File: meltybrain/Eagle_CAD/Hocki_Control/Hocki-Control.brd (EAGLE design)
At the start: 90 x 46 mm, 128 parts, among them J1 SM03B-SRSS-TB(LF)(SN), J2 SM03B-SRSS-TB(LF)(SN), J3 SM03B-SRSS-TB(LF)(SN), J4 SM04B-SRSS-TB(LF)(SN), J5 SM04B-SRSS-TB(LF)(SN), U1 TEENSY_4.1, U10 TLV3502AIDCNR, U11 NL27WZ32USG, U12 NL27WZ32USG, U13 HMC1052L-TR, U14 LMV358, U15 IRF7509, U16 TMUX1219DCKR, U17 LMV358, U18 LMV358, U19 AP2210K-3.3TRG1, U2 ADXL375, U20 AP2210K-5.0TRG1, U21 AP63200, U22 74AHC1G04GW,125, U23 LDL212PU50R, U3 ADXL375, U4 ADXL375, U5 ADXL375, U6 LMH6612MAX/NOPB, U7 LMH6612MAX/NOPB, U8 LMH6612MAX/NOPB, U9 LMH6612MAX/NOPB

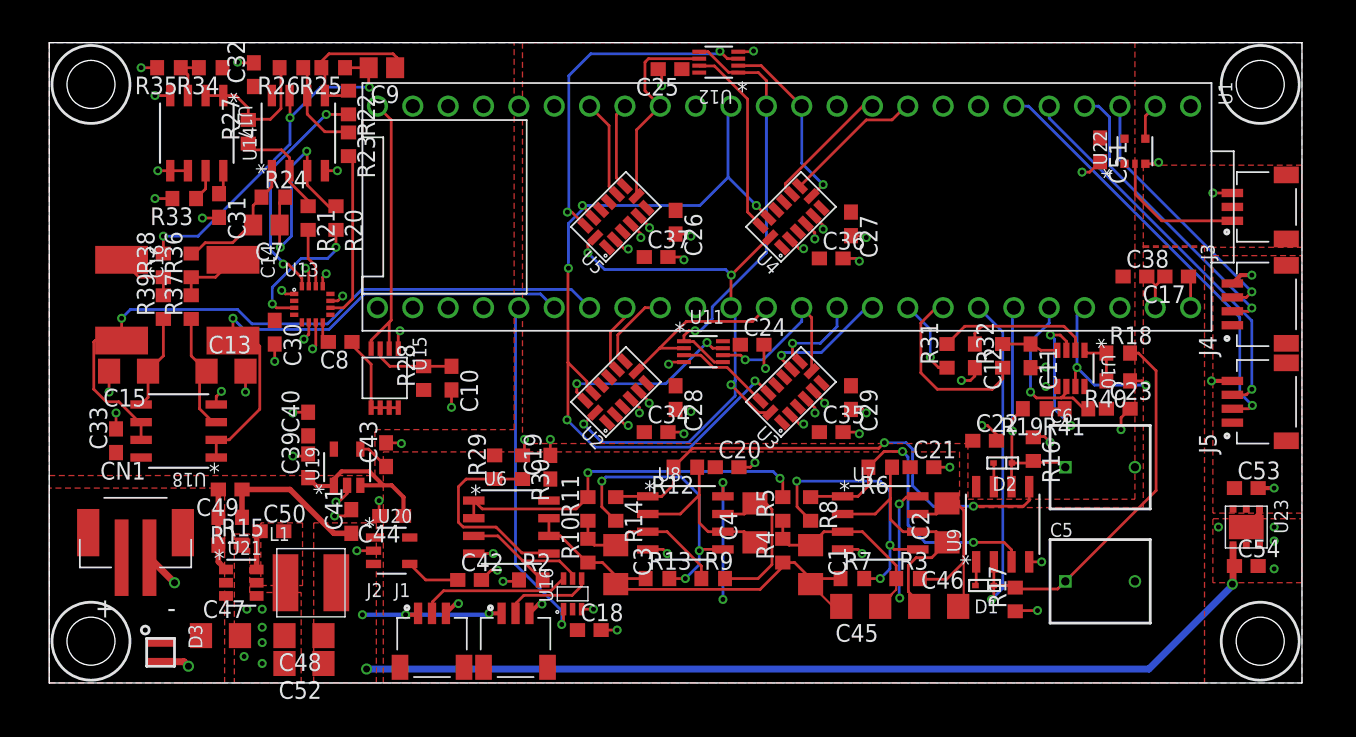
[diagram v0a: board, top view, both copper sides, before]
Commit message: control schematic done
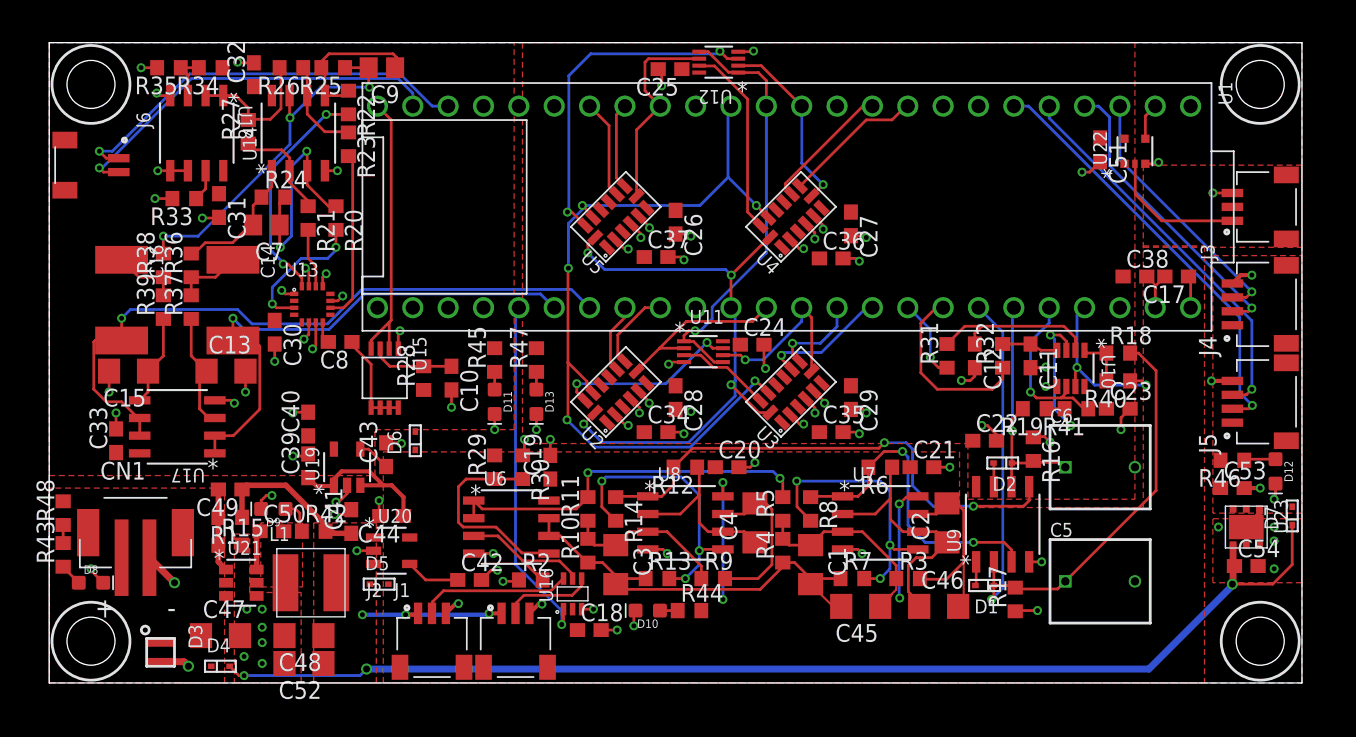
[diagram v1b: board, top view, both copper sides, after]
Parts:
- added D10, D11, D12, D13, D8, D9: GREEN, SparkFun-LED:LED-0603
- added D4, D5, D6, D7: BAS581-02V-V-G-08, Hocki_Library:SOD-523
- added J6: SM02B-SRSS-TB(LF)(SN), Hocki_Library:SM02B-SRSS-TB(LF)(SN)
- added R42: 499, rcl:R0603
- added R43, R48: 665, rcl:R0603
- added R44, R46: 330, rcl:R0603
- added R45, R47: 169, rcl:R0603
- C1, C13, C15, C2, C3, C4, C45, C46: value 47n -> 47nF
- C11, C12, C39, C41, C54: value 1u -> 1uF
- C14, C16: value 0.18u -> 0.18uF
- C17, C18, C19, C20, C21, C22, C23, C24, C25, C26, C27, C28, C29, C30, C31, C32, C33, C34, C35, C36, C37, C38, C50: value 0.1u -> 0.1uF
- C40, C44: value 2.2u -> 2.2uF
- C42, C43, C49: value 100p -> 100pF
- C47: value 10u -> 10uF
- C48, C52: value 22u -> 22uF
- C5, C6: value 62n -> 62nF
- C53: value 4.7u -> 4.7uF
- C7, C9: value 1000p -> 1000pF
- C8: value .1u -> .1uF
- moved U18 21.4 mm to (-41.4, 12.3), turned to 270 degrees
- moved U17 21.1 mm to (-42.8, -8.80), turned to 180 degrees
- moved C53 1.00 mm to (33.0, -13.2)
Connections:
- net N$17 renamed RC_SIGNAL
- new net ESC_L: J6.1, U1.30
- new net ESC_R: J6.2, U1.31
- new net N$14: D12.A, R46.1
- new net N$15: D10.A, R44.1
- new net N$17: D11.A, R45.1
- new net N$18: D9.A, R42.1
- new net N$19: D8.A, R43.1
- new net N$20: R43.2, R48.1
- new net N$27: D13.A, R47.1
- net +24V: now also D4.1, R48.2
- net +3V3: now also D6.2, J6.S1, J6.S2, R45.2
- net +5V: now also D7.2, R46.2
- net 3.3V: now also R47.2
- net 5V: now also D5.2, D6.1, R44.2
- net 9V: now also D4.2, D5.1, D7.1, R42.2
- net GND: now also D10.C, D11.C, D12.C, D13.C, D8.C, D9.C, U18.5, U18.6; no longer U17.5, U17.6
- net MAG_FILT_A: now also U17.1, U17.2; no longer U18.1, U18.2
- net MAG_FILT_B: now also U17.6, U17.7; no longer U18.6, U18.7
- net N$23: now also U18.3; no longer U17.3
- net N$24: now also U18.7; no longer U17.7
- net N$26: now also U17.3; no longer U18.3
- net N$30: now also U17.5; no longer U18.5
- net VREF/2: now also U18.1, U18.2; no longer U17.1, U17.2
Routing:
- net ESC_L: track 0.00 -> 29.9 mm, vias 0 -> 1
- net ESC_R: track 0.00 -> 28.1 mm, vias 0 -> 1
- net 9V: track 89.8 -> 108.1 mm, vias 5 -> 6
- net GND: track 111.7 -> 119.5 mm, vias 90 -> 96
- net N$18: track 0.00 -> 2.51 mm
- net N$14: track 0.00 -> 2.28 mm
- net +3V3: track 1.78 -> 0.00 mm
- net N$19: track 0.00 -> 1.62 mm
- net N$20: track 0.00 -> 1.30 mm
- net N$27: track 0.00 -> 1.27 mm
- net N$17: track 0.00 -> 1.27 mm
- net N$15: track 0.00 -> 1.27 mm

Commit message: Edited silkscreen and made minor changes to IR Receiver silkscreen and schematic
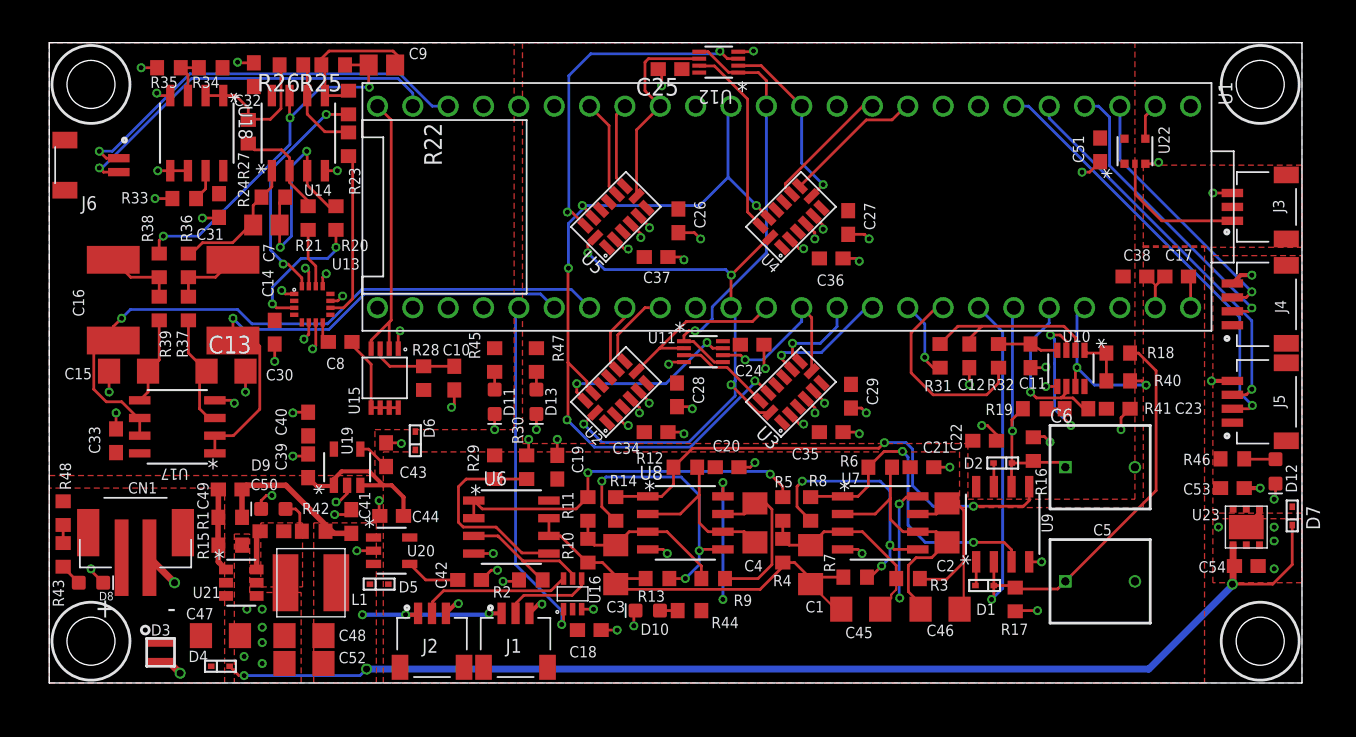
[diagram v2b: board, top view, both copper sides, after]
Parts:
- moved C16 0.60 mm to (-47.4, 0.30)
- moved C19 0.50 mm to (-15.5, -11.7)
- moved R31 0.50 mm to (12.0, -3.70)
- moved C12 0.40 mm to (14.1, -3.70)
- moved R39 0.32 mm to (-44.1, -0.30)
- moved R38 0.30 mm to (-44.1, 2.80)
- moved R30 0.30 mm to (-17.7, -11.7)
- moved R32 0.30 mm to (16.2, -3.70)
- moved R37 0.22 mm to (-42.0, -0.30)
- moved C26 0.22 mm to (-6.80, 6.00)
- moved C28 0.22 mm to (-6.90, -6.50)
- moved C27 0.22 mm to (5.40, 5.88)
- moved C46 0.22 mm to (12.0, -21.9)
- moved R7 0.22 mm to (5.90, -19.6)
- moved C10 0.20 mm to (-22.9, -5.30)
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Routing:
- net N$22: track 13.1 -> 14.3 mm
- net N$7: track 20.1 -> 19.2 mm
- net 10K_REF: track 12.5 -> 13.1 mm

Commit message: Edited LED board to add 3d packages.  Made cosmetic changes to Control in preparation for design review
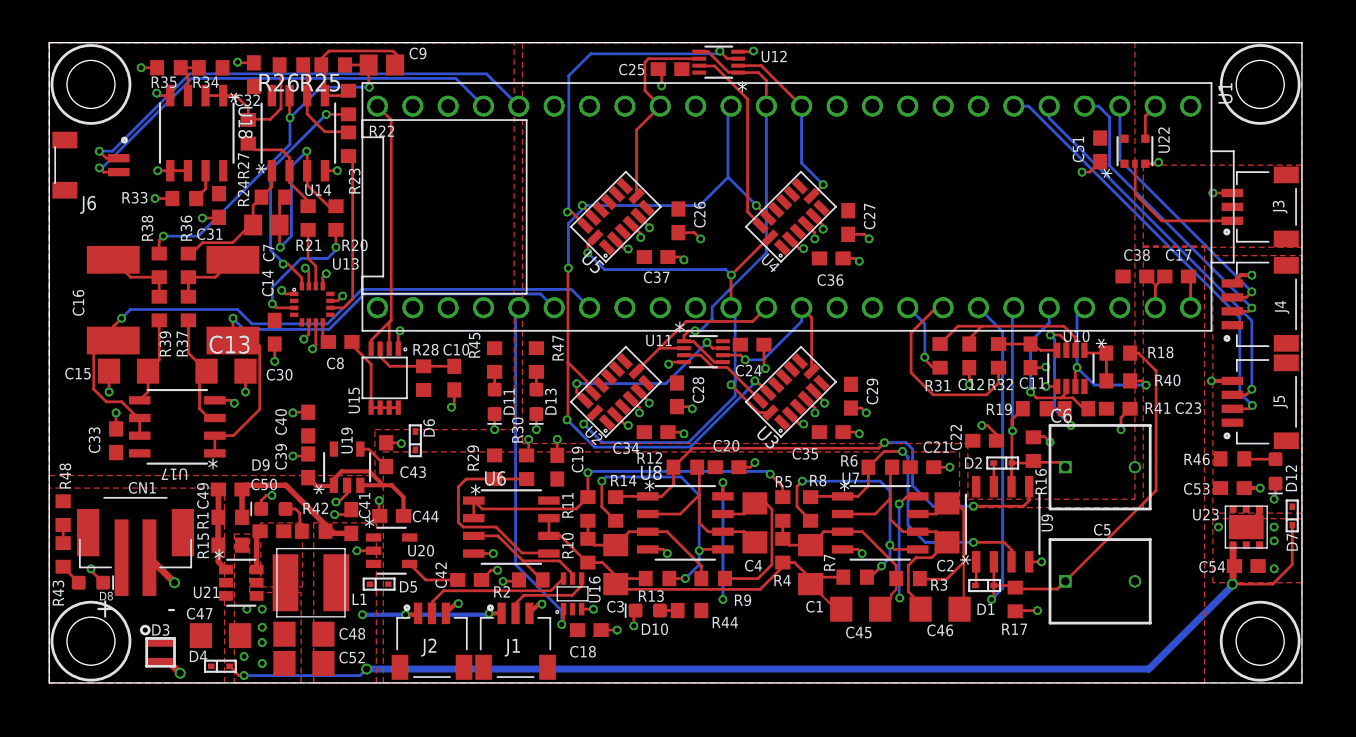
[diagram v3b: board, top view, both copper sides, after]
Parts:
- moved C48 0.10 mm to (-33.7, -23.7)
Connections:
- removed net INT1A: U1.41, U2.8
- removed net INT1B: U1.40, U2.9
- removed net INT2A: U1.16, U3.8
- removed net INT2B: U1.17, U3.9
- removed net INT3A: U1.7, U4.8
- removed net INT3B: U1.8, U4.9
- removed net INT4A: U1.25, U5.8
- removed net INT4B: U1.26, U5.9
- net 9V: now also U23.6
- net ESC_L: now also U1.28; no longer U1.30
- net ESC_R: now also U1.29; no longer U1.31
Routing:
- net INT3A: track 10.1 -> 0.00 mm
- net INT3B: track 9.50 -> 0.00 mm
- net INT2B: track 9.27 -> 0.00 mm, vias 1 -> 0
- net INT4B: track 7.14 -> 0.00 mm
- net INT2A: track 6.57 -> 0.00 mm, vias 1 -> 0
- net INT4A: track 6.26 -> 0.00 mm
- net INT1A: track 5.97 -> 0.00 mm
- net ESC_L: track 29.9 -> 35.0 mm
- net INT1B: track 5.05 -> 0.00 mm
- net ESC_R: track 28.1 -> 32.6 mm

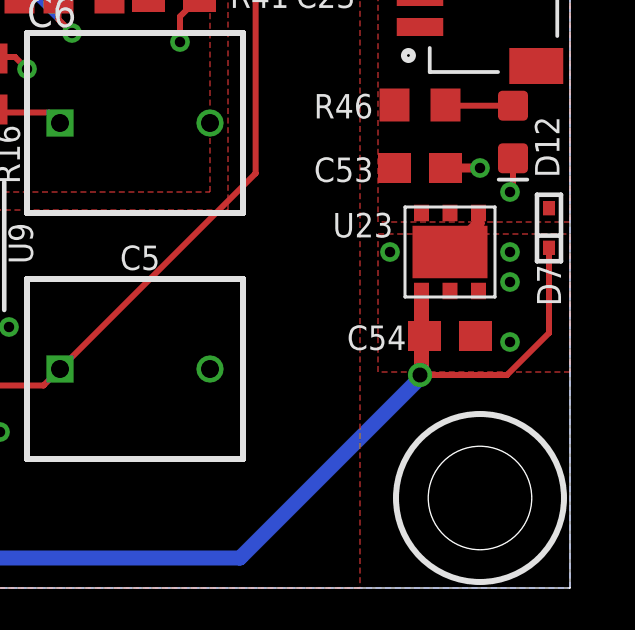
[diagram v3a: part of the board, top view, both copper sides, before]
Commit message: enable of ldo routed
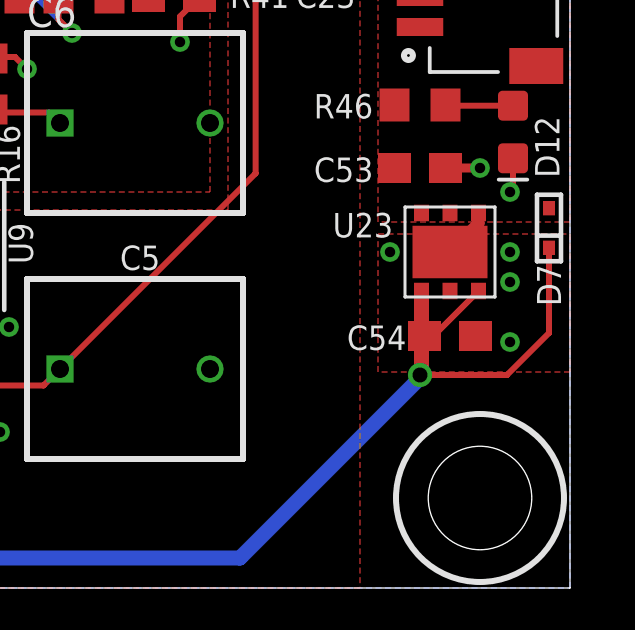
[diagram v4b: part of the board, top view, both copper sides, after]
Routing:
- net 9V: track 108.1 -> 110.7 mm
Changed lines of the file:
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@@
 <contactref element="R42" pad="2"/>
 <contactref element="U23" pad="6"/>
-<wire x1="33.05" y1="-17.3" x2="34.95" y2="-17.3" width="0" layer="19" extent="1-1"/>
+<wire x1="34.95" y1="-17.3" x2="33.35" y2="-18.9" width="0.2" layer="1"/>
+<wire x1="33.35" y1="-18.9" x2="33.05" y2="-18.9" width="0.2" layer="1"/>
 </signal>
 <signal name="N$8">

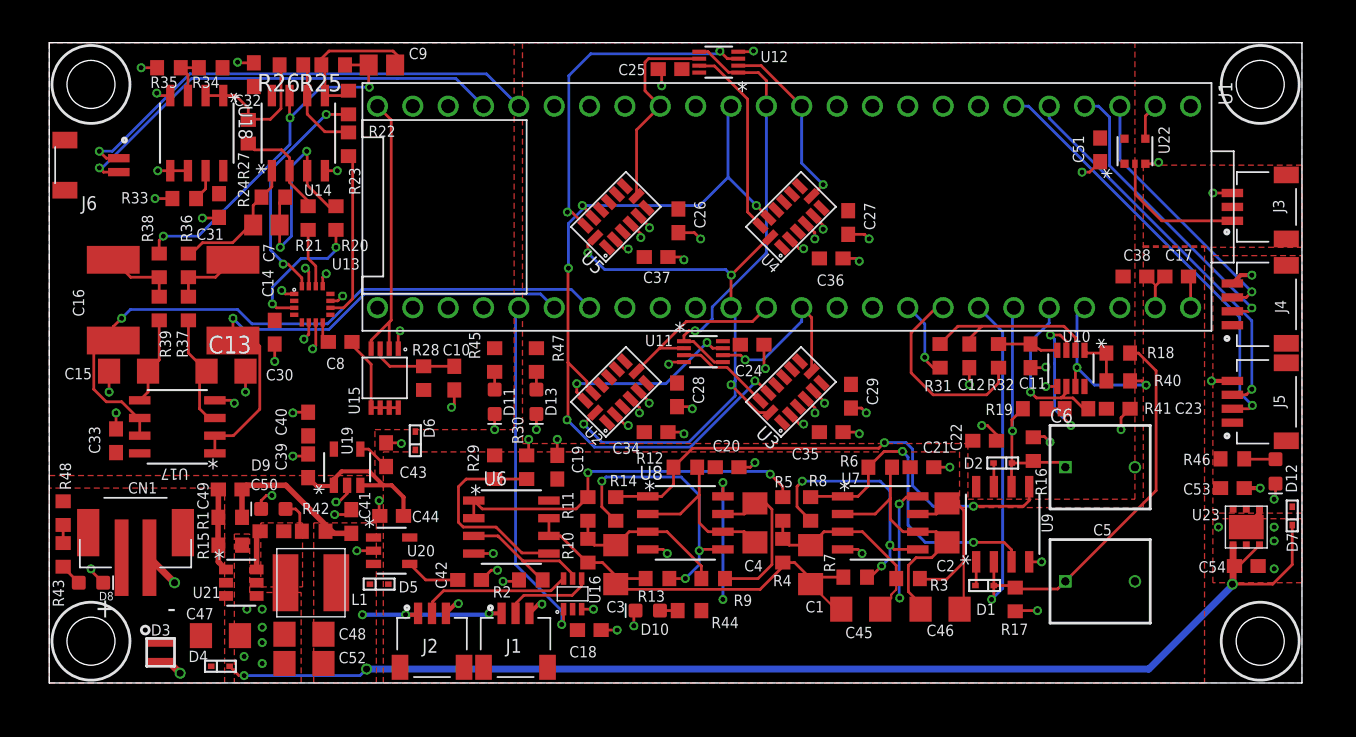
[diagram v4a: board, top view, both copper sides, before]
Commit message: control now 4 layers. silkscreen really needs work tho
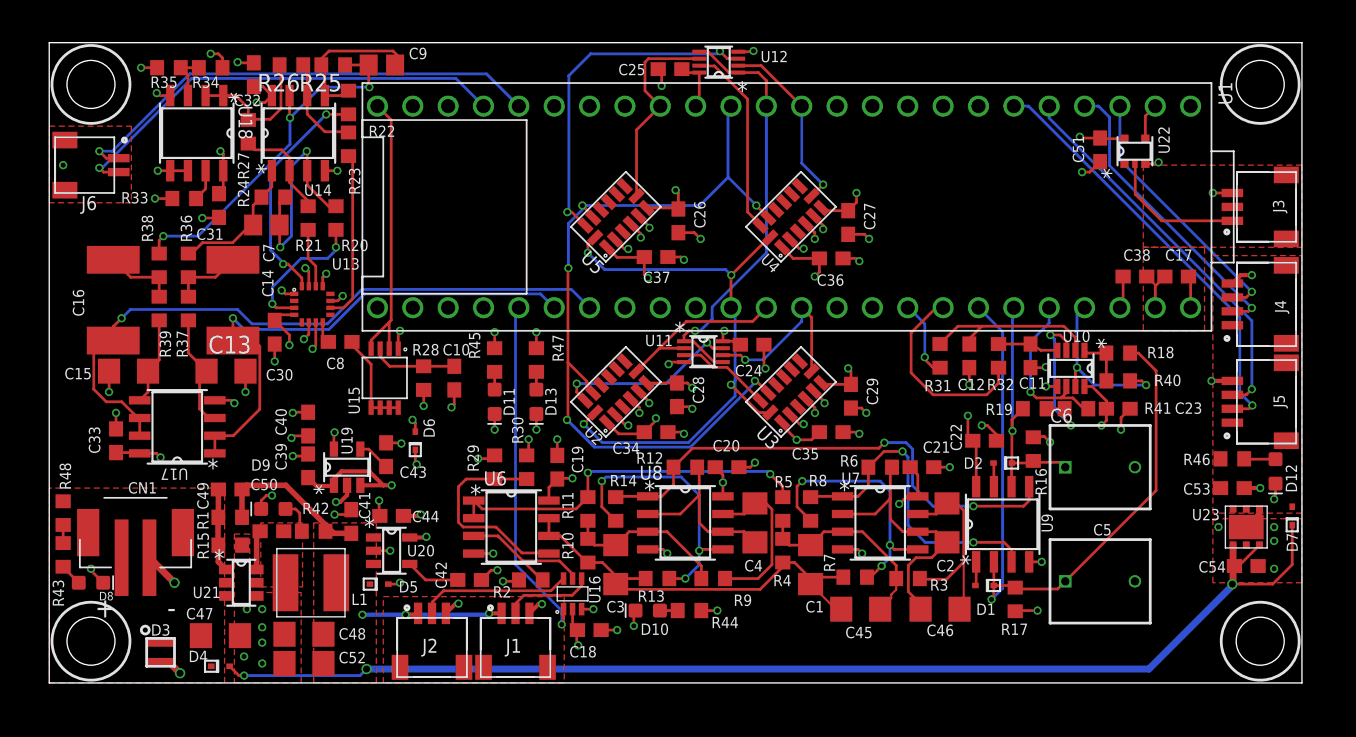
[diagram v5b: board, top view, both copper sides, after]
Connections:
- net +3V3: no longer J6.S1, J6.S2
- net 5V: no longer J1.S1, J1.S2, J2.S1, J2.S2
- net GND: now also J1.S1, J1.S2, J2.S1, J2.S2, J6.S1, J6.S2
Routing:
- net 3.3V: track 0.00 -> 53.1 mm, vias 0 -> 13
- net +3V3: track 0.00 -> 20.6 mm, vias 0 -> 10
- net 5V: track 31.6 -> 30.1 mm, vias 4 -> 11
- net GND: track 119.8 -> 119.9 mm, vias 96 -> 97
- added copper zone on layer 15, net +3V3
- added copper zone on layer 15, net 3.3V
- added copper zone on layer 15, net 5V
- added copper zone on layer 2, net GND
- removed copper zone on layer 1, net +3V3
- removed copper zone on layer 1, net 3.3V
- removed copper zone on layer 16, net GND

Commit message: added tvs diodes and did some silkscreen
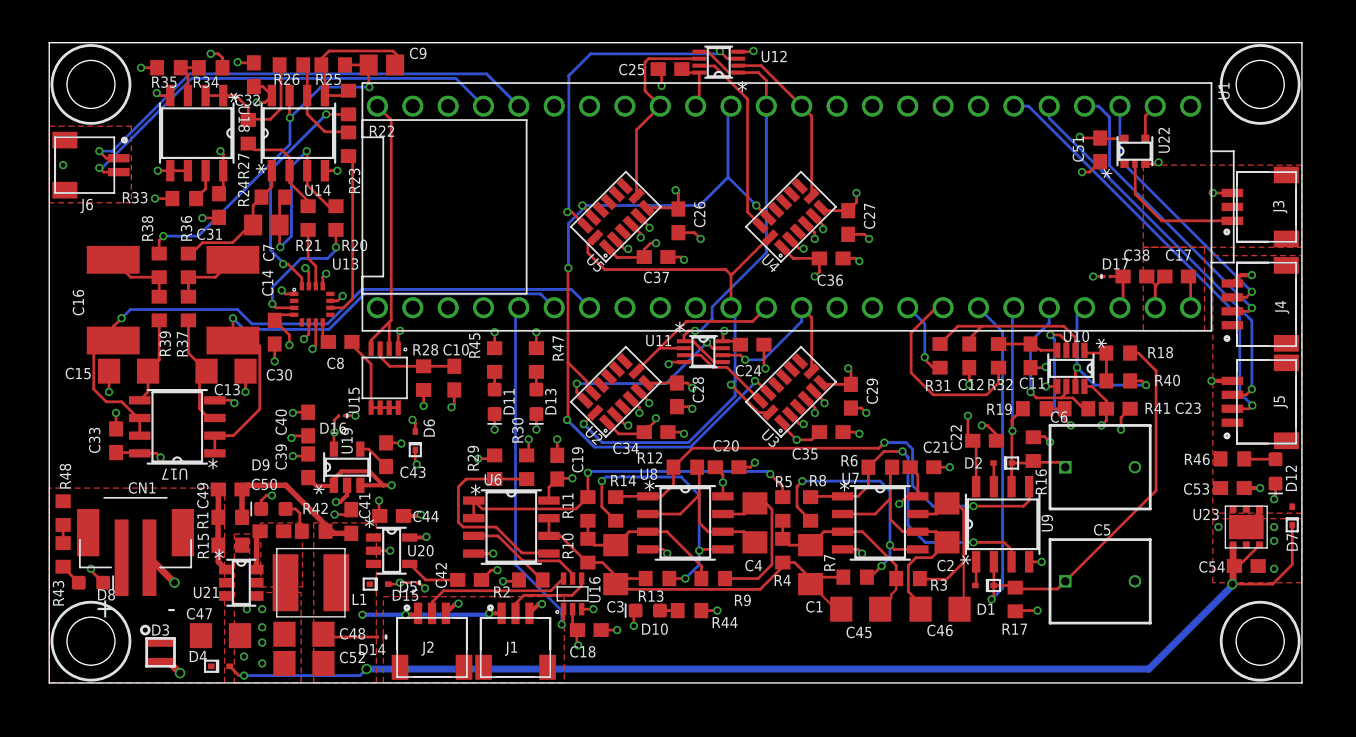
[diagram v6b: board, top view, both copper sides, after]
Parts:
- added D14: ESDZX051-1BF4, Hocki_Library:DSN0603-2
- added D15: PESD5V0H1BSFYL, Hocki_Library:DSN0603-2
- added D16, D17: PESD4V0Y1BSFYL, Hocki_Library:DSN0603-2
- C10: value 1u -> 1uF
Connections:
- net +3V3: now also D16.C2
- net 3.3V: now also D17.C2
- net 5V: now also D15.C2
- net 9V: now also D14.C2
- net GND: now also D14.C1, D15.C1, D16.C1, D17.C1
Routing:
- net 9V: track 110.7 -> 114.7 mm
- net GND: track 119.9 -> 122.3 mm, vias 97 -> 100
- net +3V3: track 20.6 -> 22.0 mm
- net 3.3V: track 53.1 -> 54.1 mm
- net 5V: track 30.1 -> 30.9 mm
- net CS3: track 13.2 -> 12.5 mm, vias 1 -> 0
- net SCLK: vias 4 -> 2
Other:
- board text added: "+"
